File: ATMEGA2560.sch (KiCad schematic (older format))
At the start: 20 parts, among them U1 ATmega2560-16AU

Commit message: added endstops
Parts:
- added J? (x2): Conn_02x06_Odd_Even, symbol Connector_Generic:Conn_02x06_Odd_Even
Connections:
- net labels added: +5V
- wire segments 172 -> 208
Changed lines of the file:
@@
 $Descr A4 11693 8268
 encoding utf-8
-Sheet 5 8
+Sheet 8 8
 Title ""
 Date ""
@@
 Text HLabel 5650 6600 2    59   Input ~ 0
 P_1_I
-Text HLabel 5650 6700 2    59   Input ~ 0
+Text HLabel 6250 5050 2    59   Input ~ 0
 P_2_I
-Text HLabel 5650 6800 2    59   Input ~ 0
+Text HLabel 6250 5150 2    59   Input ~ 0
 P_3_I
 Wire Wire Line
@@
 Wire Wire Line
 	2150 6500 3700 6500
-Wire Wire Line
-	3100 4000 3850 4000
-Wire Wire Line
-	3100 4100 3850 4100
-Wire Wire Line
-	3100 4200 3850 4200
-Wire Wire Line
-	3100 4300 3850 4300
-Wire Wire Line
-	3100 4400 3850 4400
-Wire Wire Line
-	3100 4500 3850 4500
 $Comp
 L Device:R R?
@@
 Wire Wire Line
 	1550 2900 1550 3000
+Wire Wire Line
+	3100 4500 3850 4500
+Wire Wire Line
+	3100 4400 3850 4400
+Wire Wire Line
+	3100 4300 3850 4300
+Wire Wire Line
+	3100 4200 3850 4200
+Wire Wire Line
+	3100 4100 3850 4100
+Wire Wire Line
+	3100 4000 3850 4000
+$Comp
+L Connector_Generic:Conn_02x06_Odd_Even J?
+U 1 1 62EF8F2F
+P 9200 5450
+F 0 "J?" H 9250 5867 50  0000 C CNN
+F 1 "Conn_02x06_Odd_Even" H 9250 5776 50  0000 C CNN
+F 2 "" H 9200 5450 50  0001 C CNN
+F 3 "~" H 9200 5450 50  0001 C CNN
+	1    9200 5450
+	1    0    0    -1
+$EndComp
+$Comp
+L Connector_Generic:Conn_02x06_Odd_Even J?
+U 1 1 62EF965D
+P 10050 5450
+F 0 "J?" H 10100 5867 50  0000 C CNN
+F 1 "Conn_02x06_Odd_Even" H 10100 5776 50  0000 C CNN
+F 2 "" H 10050 5450 50  0001 C CNN
+F 3 "~" H 10050 5450 50  0001 C CNN
+	1    10050 5450
+	1    0    0    -1
+$EndComp
+Text Label 10850 5250 2    59   ~ 0
+X_MIN
+Text Label 10850 5350 2    59   ~ 0
+X_MAX
+Text Label 10850 5550 2    59   ~ 0
+Y_MAX
+Text Label 10850 5450 2    59   ~ 0
+Y_MIN
+Text Label 10850 5750 2    59   ~ 0
+Z_MAX
+Text Label 10850 5650 2    59   ~ 0
+Z_MIN
+Wire Wire Line
+	10350 5750 11100 5750
+Wire Wire Line
+	10350 5650 11100 5650
+Wire Wire Line
+	10350 5550 11100 5550
+Wire Wire Line
+	10350 5450 11100 5450
+Wire Wire Line
+	10350 5350 11100 5350
+Wire Wire Line
+	10350 5250 11100 5250
+$Comp
+L power:GND #PWR?
+U 1 1 62F30E7C
+P 9650 6100
+F 0 "#PWR?" H 9650 5850 50  0001 C CNN
+F 1 "GND" H 9655 5927 50  0000 C CNN
+F 2 "" H 9650 6100 50  0001 C CNN
+F 3 "" H 9650 6100 50  0001 C CNN
+	1    9650 6100
+	1    0    0    -1
+$EndComp
+Wire Wire Line
+	9500 5250 9650 5250
+Wire Wire Line
+	9500 5350 9650 5350
+Wire Wire Line
+	9850 5450 9650 5450
+Wire Wire Line
+	9500 5550 9650 5550
+Wire Wire Line
+	9850 5650 9650 5650
+Wire Wire Line
+	9500 5750 9650 5750
+Wire Wire Line
+	9650 6100 9650 5750
+Connection ~ 9650 5250
+Wire Wire Line
+	9650 5250 9850 5250
+Connection ~ 9650 5350
+Wire Wire Line
+	9650 5350 9850 5350
+Wire Wire Line
+	9650 5350 9650 5250
+Connection ~ 9650 5450
+Wire Wire Line
+	9650 5450 9500 5450
+Wire Wire Line
+	9650 5450 9650 5350
+Connection ~ 9650 5550
+Wire Wire Line
+	9650 5550 9850 5550
+Wire Wire Line
+	9650 5550 9650 5450
+Connection ~ 9650 5650
+Wire Wire Line
+	9650 5650 9500 5650
+Wire Wire Line
+	9650 5650 9650 5550
+Connection ~ 9650 5750
+Wire Wire Line
+	9650 5750 9850 5750
+Wire Wire Line
+	9650 5750 9650 5650
+$Comp
+L power:+5V #PWR?
+U 1 1 62F81107
+P 8550 5150
+F 0 "#PWR?" H 8550 5000 50  0001 C CNN
+F 1 "+5V" H 8565 5323 50  0000 C CNN
+F 2 "" H 8550 5150 50  0001 C CNN
+F 3 "" H 8550 5150 50  0001 C CNN
+	1    8550 5150
+	1    0    0    -1
+$EndComp
+Wire Wire Line
+	9000 5750 8550 5750
+Wire Wire Line
+	8550 5750 8550 5650
+Wire Wire Line
+	9000 5250 8550 5250
+Connection ~ 8550 5250
+Wire Wire Line
+	8550 5250 8550 5150
+Wire Wire Line
+	8550 5350 9000 5350
+Connection ~ 8550 5350
+Wire Wire Line
+	8550 5350 8550 5250
+Wire Wire Line
+	9000 5450 8550 5450
+Connection ~ 8550 5450
+Wire Wire Line
+	8550 5450 8550 5350
+Wire Wire Line
+	8550 5550 9000 5550
+Connection ~ 8550 5550
+Wire Wire Line
+	8550 5550 8550 5450
+Wire Wire Line
+	9000 5650 8550 5650
+Connection ~ 8550 5650
+Wire Wire Line
+	8550 5650 8550 5550
 Wire Bus Line
 	1000 550  1000 1500

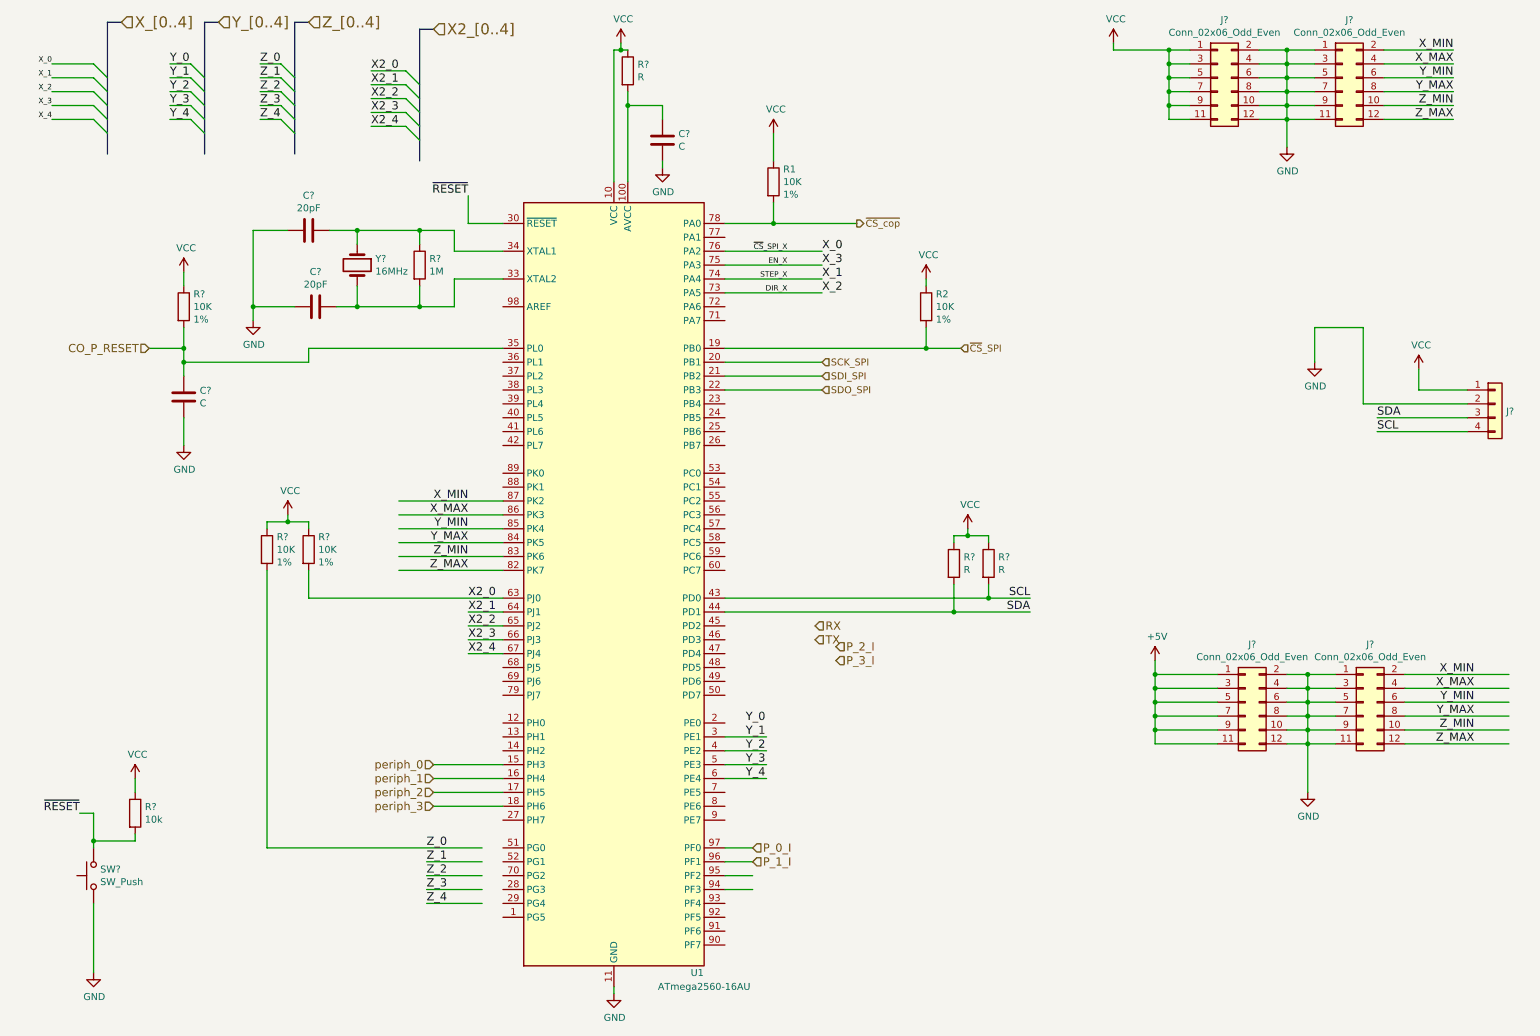
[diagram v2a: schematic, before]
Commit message: removed osc from CoP. added signals to atmega
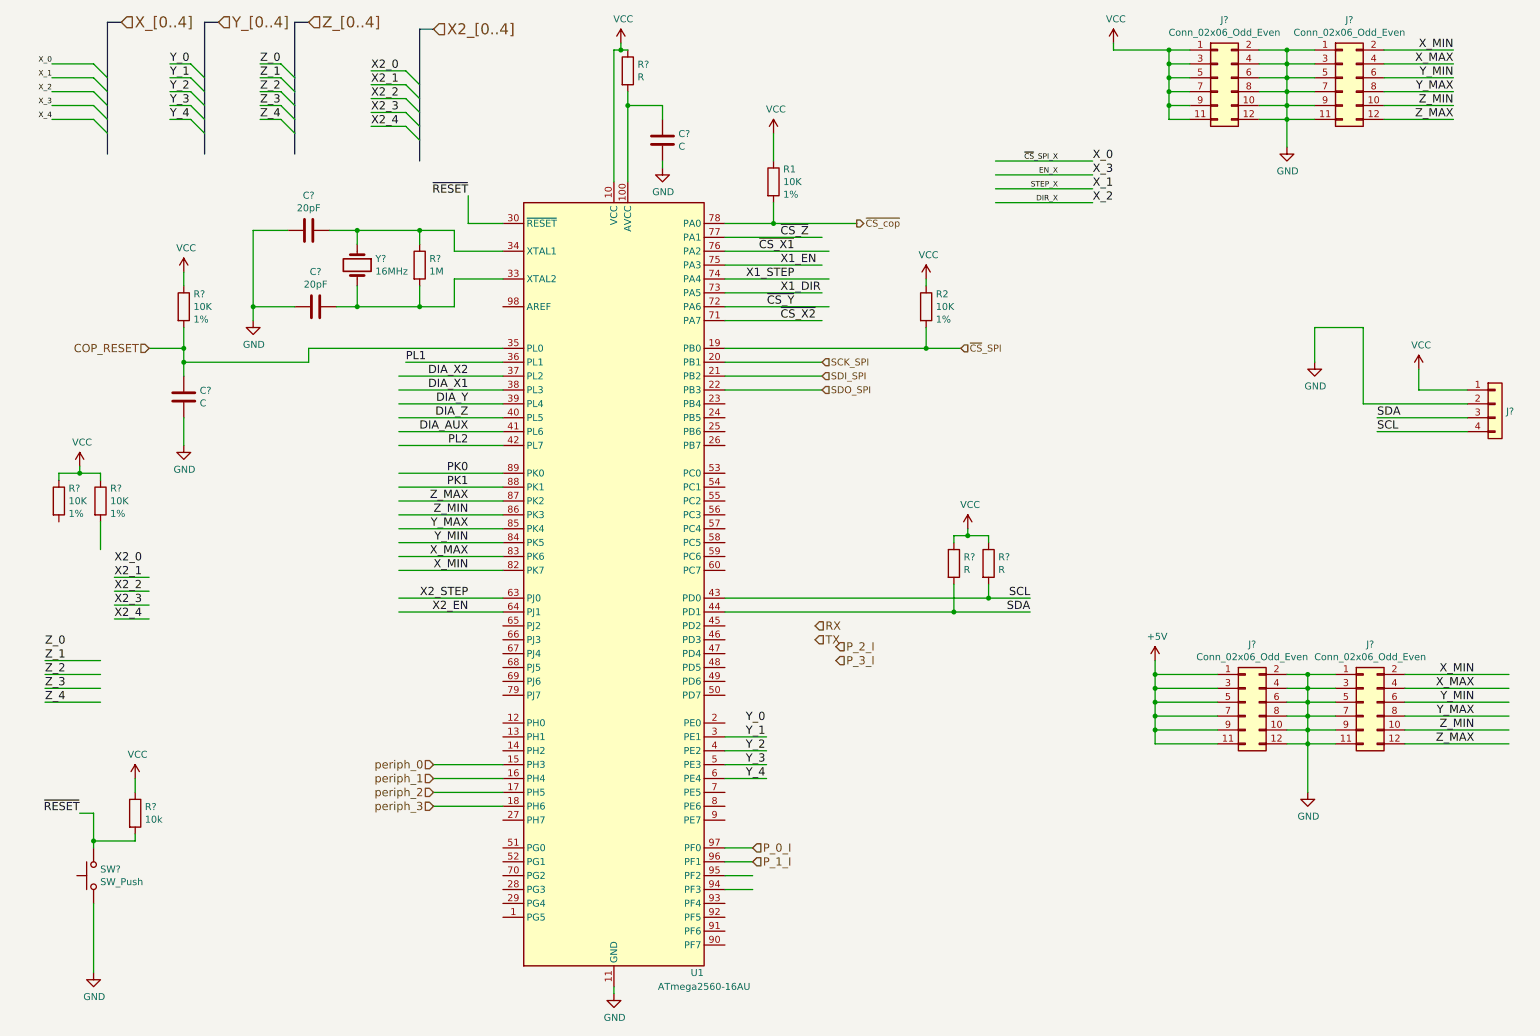
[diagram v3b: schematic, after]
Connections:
- net labels added: COP_RESET, DIA_AUX, DIA_X1, DIA_X2, DIA_Y, DIA_Z, PK0, PK1, PL1, PL2, X1_DIR, X1_EN, X1_STEP, X2_EN, X2_STEP, ~CS_X1, ~CS_X2, ~CS_Y, ~CS_Z
- net labels removed: CO_P_RESET
- wire segments 208 -> 223
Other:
- moved on the sheet: R?
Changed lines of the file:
@@
 Text Label 5600 6000 0    59   ~ 0
 Y_4
-Text Label 3300 6500 0    59   ~ 0
+Text Label 550  5050 0    59   ~ 0
 Z_0
-Text Label 3300 6600 0    59   ~ 0
+Text Label 550  5150 0    59   ~ 0
 Z_1
-Text Label 3300 6700 0    59   ~ 0
+Text Label 550  5250 0    59   ~ 0
 Z_2
-Text Label 3300 6800 0    59   ~ 0
+Text Label 550  5350 0    59   ~ 0
 Z_3
-Text Label 3300 6900 0    59   ~ 0
+Text Label 550  5450 0    59   ~ 0
 Z_4
 Wire Wire Line
@@
 	5450 6000 5750 6000
 Wire Wire Line
-	3300 6600 3700 6600
-Wire Wire Line
-	3300 6700 3700 6700
-Wire Wire Line
-	3300 6800 3700 6800
-Wire Wire Line
-	3300 6900 3700 6900
+	550  5150 950  5150
+Wire Wire Line
+	550  5250 950  5250
+Wire Wire Line
+	550  5350 950  5350
+Wire Wire Line
+	550  5450 950  5450
 Wire Wire Line
 	2900 900  3150 900
@@
 X2_4
 Wire Wire Line
-	3600 4800 3850 4800
-Wire Wire Line
-	3600 4900 3850 4900
-Wire Wire Line
-	3600 5000 3850 5000
-Wire Wire Line
-	3600 5100 3850 5100
-Text Label 3600 4700 0    59   ~ 0
+	1050 4550 1300 4550
+Wire Wire Line
+	1050 4650 1300 4650
+Wire Wire Line
+	1050 4750 1300 4750
+Wire Wire Line
+	1050 4850 1300 4850
+Text Label 1050 4450 0    59   ~ 0
 X2_0
-Text Label 3600 4800 0    59   ~ 0
+Text Label 1050 4550 0    59   ~ 0
 X2_1
-Text Label 3600 4900 0    59   ~ 0
+Text Label 1050 4650 0    59   ~ 0
 X2_2
-Text Label 3600 5000 0    59   ~ 0
+Text Label 1050 4750 0    59   ~ 0
 X2_3
-Text Label 3600 5100 0    59   ~ 0
+Text Label 1050 4850 0    59   ~ 0
 X2_4
 Text HLabel 5650 6500 2    59   Input ~ 0
@@
 Wire Wire Line
 	5450 6800 5650 6800
-Text Label 6150 2400 0    59   ~ 0
+Text Label 8100 1750 0    59   ~ 0
 X_1
-Text Label 6150 2500 0    59   ~ 0
+Text Label 8100 1850 0    59   ~ 0
 X_2
 Wire Wire Line
-	6150 2400 5450 2400
-Wire Wire Line
-	6150 2500 5450 2500
-Text Label 5900 2400 2    39   ~ 0
+	8100 1750 7400 1750
+Wire Wire Line
+	8100 1850 7400 1850
+Text Label 7850 1750 2    39   ~ 0
 STEP_X
-Text Label 5900 2500 2    39   ~ 0
+Text Label 7850 1850 2    39   ~ 0
 DIR_X
-Text Label 6150 2300 0    59   ~ 0
+Text Label 8100 1650 0    59   ~ 0
 X_3
 Wire Wire Line
-	6150 2300 5450 2300
-Text Label 5900 2300 2    39   ~ 0
+	8100 1650 7400 1650
+Text Label 7850 1650 2    39   ~ 0
 EN_X
-Text Label 6150 2200 0    59   ~ 0
+Text Label 8100 1550 0    59   ~ 0
 X_0
 Wire Wire Line
-	6150 2200 5450 2200
-Text Label 5900 2200 2    39   ~ 0
+	8100 1550 7400 1550
+Text Label 7850 1550 2    39   ~ 0
 ~CS~_SPI_X
 $Comp
@@
 L Device:R R?
 U 1 1 6219C526
-P 2450 4350
-F 0 "R?" H 2520 4441 50  0000 L CNN
-F 1 "10K" H 2520 4350 50  0000 L CNN
-F 2 "" V 2380 4350 50  0001 C CNN
-F 3 "~" H 2450 4350 50  0001 C CNN
-F 4 "1%" H 2520 4259 50  0000 L CNN "Tolerance"
-	1    2450 4350
+P 950 4000
+F 0 "R?" H 1020 4091 50  0000 L CNN
+F 1 "10K" H 1020 4000 50  0000 L CNN
+F 2 "" V 880 4000 50  0001 C CNN
+F 3 "~" H 950 4000 50  0001 C CNN
+F 4 "1%" H 1020 3909 50  0000 L CNN "Tolerance"
+	1    950  4000
 	1    0    0    -1
 $EndComp
@@
 L Device:R R?
 U 1 1 6219E013
-P 2150 4350
-F 0 "R?" H 2220 4441 50  0000 L CNN
-F 1 "10K" H 2220 4350 50  0000 L CNN
-F 2 "" V 2080 4350 50  0001 C CNN
-F 3 "~" H 2150 4350 50  0001 C CNN
-F 4 "1%" H 2220 4259 50  0000 L CNN "Tolerance"
-	1    2150 4350
+P 650 4000
+F 0 "R?" H 720 4091 50  0000 L CNN
+F 1 "10K" H 720 4000 50  0000 L CNN
+F 2 "" V 580 4000 50  0001 C CNN
+F 3 "~" H 650 4000 50  0001 C CNN
+F 4 "1%" H 720 3909 50  0000 L CNN "Tolerance"
+	1    650  4000
 	1    0    0    -1
 $EndComp
@@
 L power:VCC #PWR?
 U 1 1 621A8082
-P 2300 4100
-F 0 "#PWR?" H 2300 3950 50  0001 C CNN
-F 1 "VCC" H 2317 4273 50  0000 C CNN
-F 2 "" H 2300 4100 50  0001 C CNN
-F 3 "" H 2300 4100 50  0001 C CNN
-	1    2300 4100
-	1    0    0    -1
-$EndComp
-Wire Wire Line
-	2450 4700 2450 4500
-Wire Wire Line
-	2450 4700 3850 4700
-Wire Wire Line
-	2150 4200 2150 4150
-Wire Wire Line
-	2150 4150 2300 4150
-Wire Wire Line
-	2450 4150 2450 4200
-Wire Wire Line
-	2300 4100 2300 4150
-Connection ~ 2300 4150
-Wire Wire Line
-	2300 4150 2450 4150
+P 800 3750
+F 0 "#PWR?" H 800 3600 50  0001 C CNN
+F 1 "VCC" H 817 3923 50  0000 C CNN
+F 2 "" H 800 3750 50  0001 C CNN
+F 3 "" H 800 3750 50  0001 C CNN
+	1    800  3750
+	1    0    0    -1
+$EndComp
+Wire Wire Line
+	950  4350 950  4150
+Wire Wire Line
+	650  3850 650  3800
+Wire Wire Line
+	650  3800 800  3800
+Wire Wire Line
+	950  3800 950  3850
+Wire Wire Line
+	800  3750 800  3800
+Connection ~ 800  3800
+Wire Wire Line
+	800  3800 950  3800
 Text HLabel 6100 5000 2    59   Input ~ 0
 TX
@@
 Text Label 10700 1150 2    59   ~ 0
 Z_MIN
+Text Label 3600 4500 2    59   ~ 0
+X_MIN
+Text Label 3600 4400 2    59   ~ 0
+X_MAX
+Text Label 3600 4200 2    59   ~ 0
+Y_MAX
+Text Label 3600 4300 2    59   ~ 0
+Y_MIN
 Text Label 3600 4000 2    59   ~ 0
-X_MIN
+Z_MAX
 Text Label 3600 4100 2    59   ~ 0
-X_MAX
-Text Label 3600 4300 2    59   ~ 0
-Y_MAX
-Text Label 3600 4200 2    59   ~ 0
-Y_MIN
-Text Label 3600 4500 2    59   ~ 0
-Z_MAX
-Text Label 3600 4400 2    59   ~ 0
 Z_MIN
 $Comp
@@
 	7150 2900 6900 2900
 Connection ~ 6900 2900
-Wire Wire Line
-	2150 4500 2150 6500
-Wire Wire Line
-	2150 6500 3700 6500
 $Comp
 L Device:R R?
@@
 $EndComp
 Text HLabel 1300 2900 0    59   Input ~ 0
-CO_P_RESET
+COP_RESET
 Wire Wire Line
 	1550 3400 1550 3600
@@
 	1550 2900 1550 3000
 Wire Wire Line
+	3100 4000 3850 4000
+Wire Wire Line
+	3100 4100 3850 4100
+Wire Wire Line
+	3100 4200 3850 4200
+Wire Wire Line
+	3100 4300 3850 4300
+Wire Wire Line
+	3100 4400 3850 4400
+Wire Wire Line
 	3100 4500 3850 4500
-Wire Wire Line
-	3100 4400 3850 4400
-Wire Wire Line
-	3100 4300 3850 4300
-Wire Wire Line
-	3100 4200 3850 4200
-Wire Wire Line
-	3100 4100 3850 4100
-Wire Wire Line
-	3100 4000 3850 4000
 $Comp
 L Connector_Generic:Conn_02x06_Odd_Even J?
@@
 Wire Wire Line
 	8550 5650 8550 5550
+Text Label 3600 3900 2    59   ~ 0
+PK1
+Text Label 3600 3800 2    59   ~ 0
+PK0
+Wire Wire Line
+	3850 3800 3100 3800
+Wire Wire Line
+	3850 3900 3100 3900
+Text Label 3600 4700 2    59   ~ 0
+X2_STEP
+Text Label 3600 4800 2    59   ~ 0
+X2_EN
+Wire Wire Line
+	3100 4800 3850 4800
+Wire Wire Line
+	3100 4700 3850 4700
+Text Label 3600 3200 2    59   ~ 0
+DIA_X1
+Text Label 3600 3100 2    59   ~ 0
+DIA_X2
+Wire Wire Line
+	3850 3100 3100 3100
+Wire Wire Line
+	3850 3200 3100 3200
+Text Label 3600 3400 2    59   ~ 0
+DIA_Z
+Text Label 3600 3300 2    59   ~ 0
+DIA_Y
+Wire Wire Line
+	3850 3300 3100 3300
+Wire Wire Line
+	3850 3400 3100 3400
+Text Label 3600 3600 2    59   ~ 0
+PL2
+Text Label 3600 3500 2    59   ~ 0
+DIA_AUX
+Wire Wire Line
+	3850 3500 3100 3500
+Wire Wire Line
+	3850 3600 3100 3600
+Text Label 3150 3000 0    59   ~ 0
+PL1
+Wire Wire Line
+	3150 3000 3850 3000
+Text Label 5950 2200 2    59   ~ 0
+~CS_X1
+Wire Wire Line
+	6200 2200 5450 2200
+Text Label 5850 2100 0    59   ~ 0
+~CS_Z
+Wire Wire Line
+	5450 2100 6150 2100
+Text Label 5950 2400 2    59   ~ 0
+X1_STEP
+Wire Wire Line
+	6200 2400 5450 2400
+Text Label 5850 2300 0    59   ~ 0
+X1_EN
+Wire Wire Line
+	5450 2300 6150 2300
+Text Label 5950 2600 2    59   ~ 0
+~CS_Y
+Wire Wire Line
+	6200 2600 5450 2600
+Text Label 5850 2500 0    59   ~ 0
+X1_DIR
+Wire Wire Line
+	5450 2500 6150 2500
+Text Label 5850 2700 0    59   ~ 0
+~CS_X2
+Wire Wire Line
+	5450 2700 6150 2700
 Wire Bus Line
 	1000 550  1000 1500
